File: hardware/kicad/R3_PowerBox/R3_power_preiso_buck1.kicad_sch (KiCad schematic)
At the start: 19 parts, among them U2 TPS54302DDCR

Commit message: Finalize R3 PowerBox pre-placement corrections
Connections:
- net N$13 renamed N$12

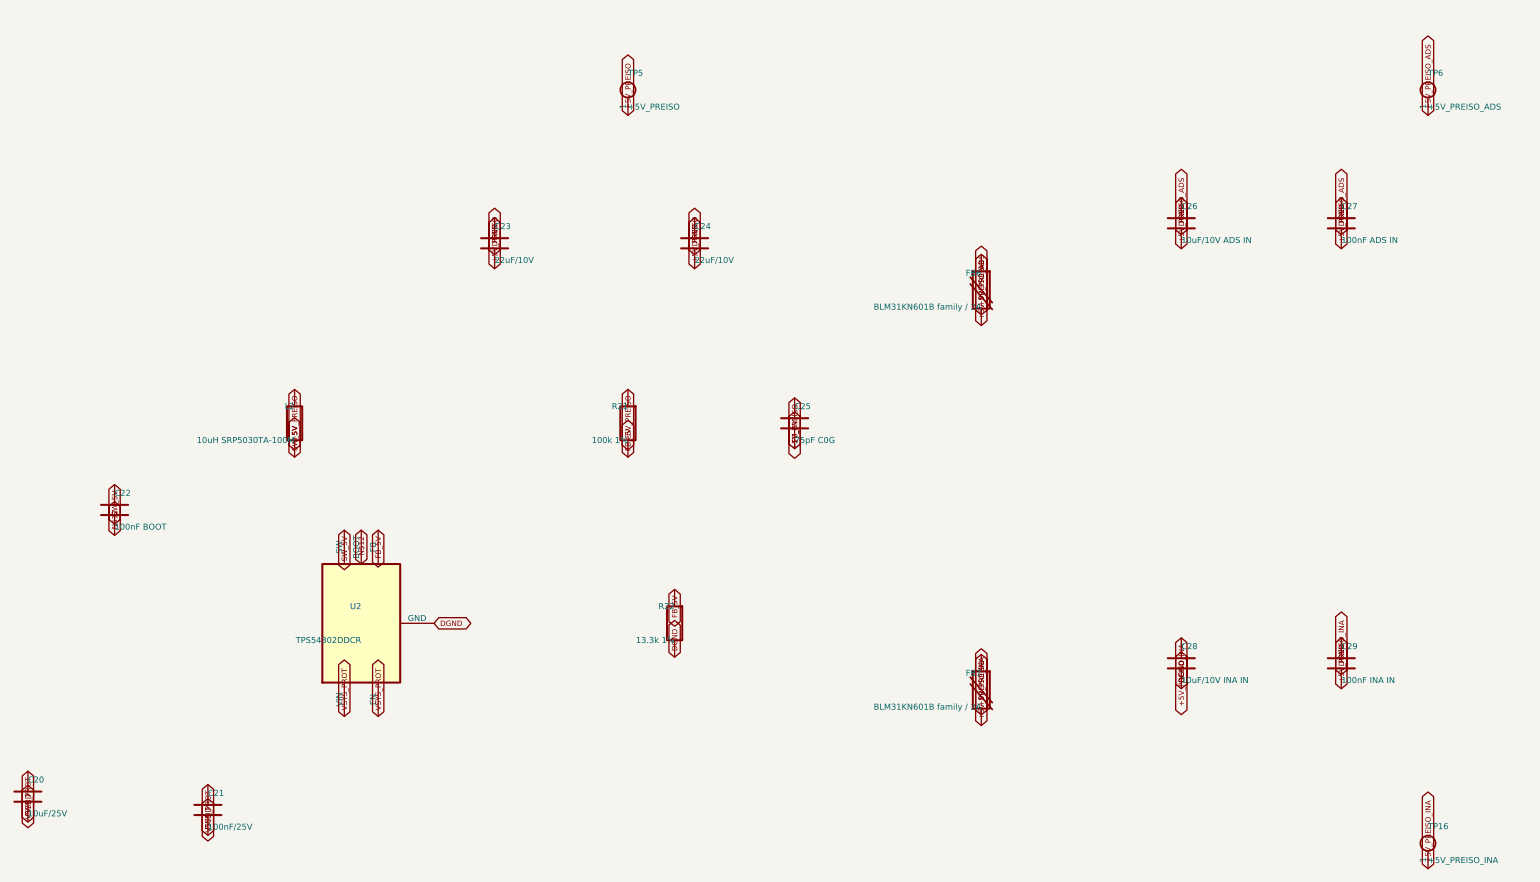
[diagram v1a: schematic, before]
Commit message: Finalize R3 PowerBox pre-routing placement
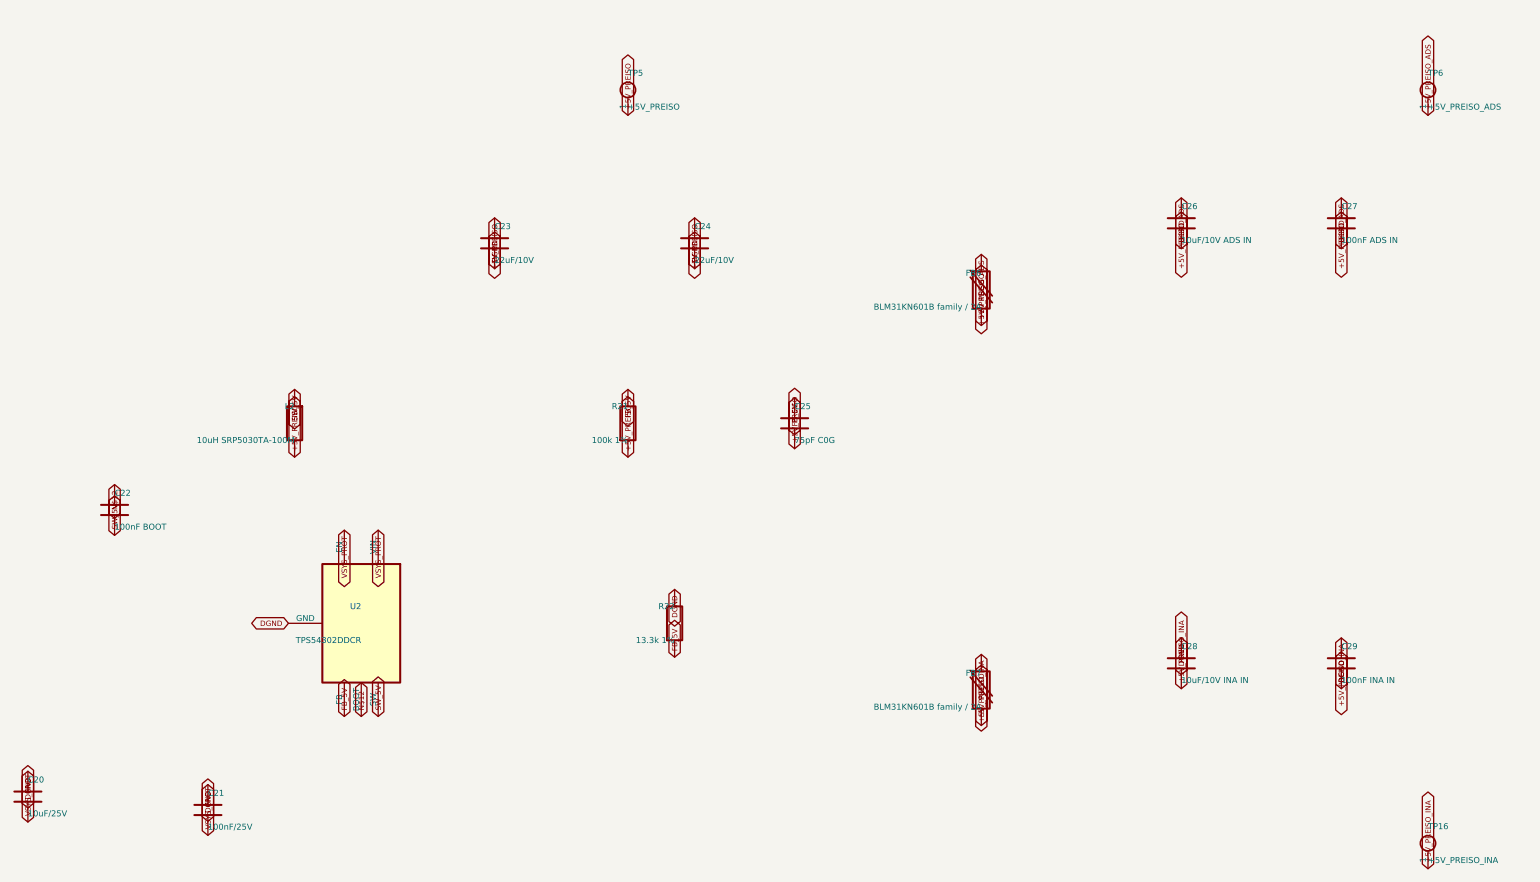
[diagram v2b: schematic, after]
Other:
- moved on the sheet: FB6, FB7, L2, R21, R22, U2

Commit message: Finalize R3 PowerBox user power controls
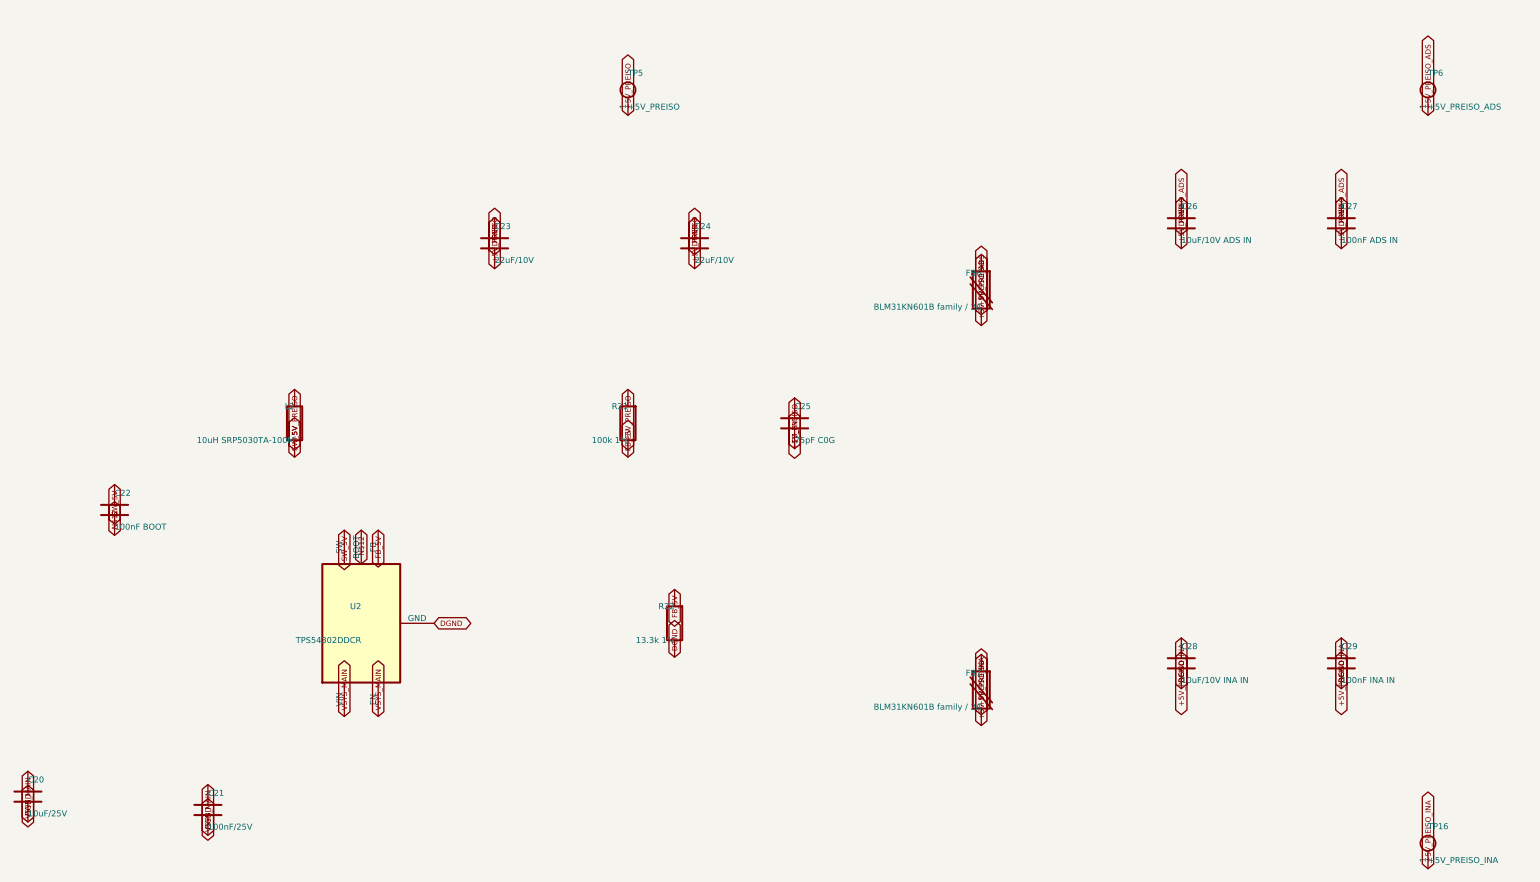
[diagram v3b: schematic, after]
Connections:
- net VSYS_PROT renamed VSYS_MAIN
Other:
- moved on the sheet: FB6, FB7, L2, R21, R22, U2

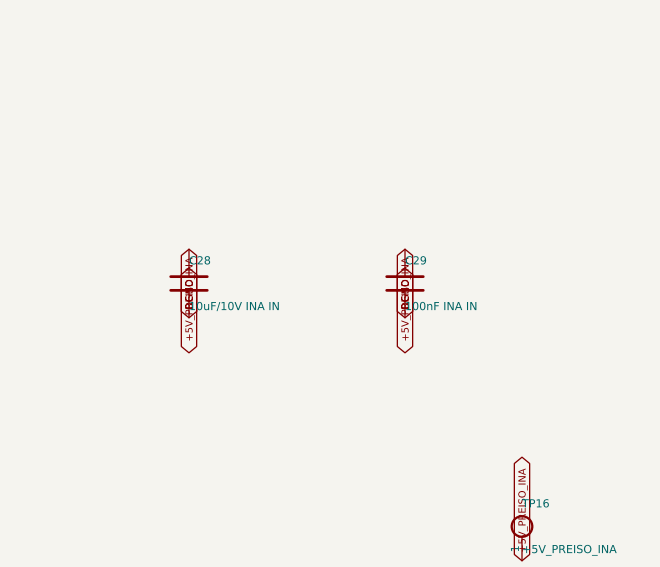
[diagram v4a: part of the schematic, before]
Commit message: Finish R3 PowerBox routing checkpoint F and verification
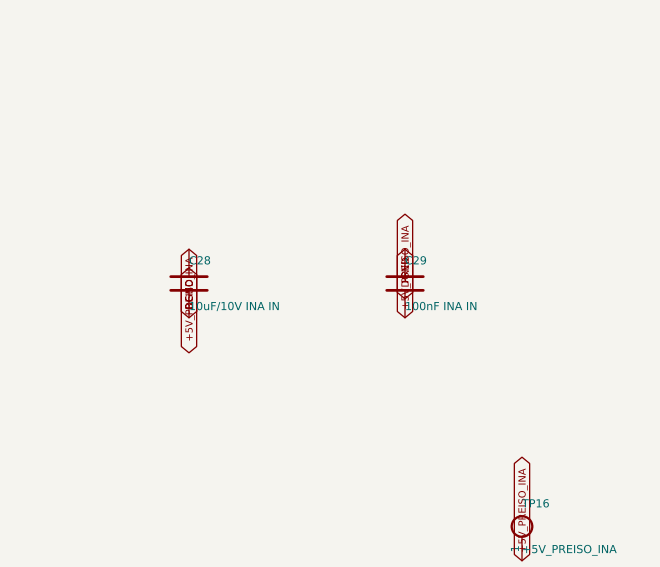
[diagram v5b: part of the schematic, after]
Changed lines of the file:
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@@
 	(global_label "+5V_PREISO_INA"
+		(shape bidirectional)
+		(at 252 131.81 90)
+		(effects
+			(font
+				(size 0.8 0.8)
+			)
+			(justify left)
+		)
+	)
+	(global_label "DGND"
 		(shape bidirectional)
 		(at 252 124.19 270)
@@
 			)
 			(justify right)
-		)
-	)
-	(global_label "DGND"
-		(shape bidirectional)
-		(at 252 131.81 90)
-		(effects
-			(font
-				(size 0.8 0.8)
-			)
-			(justify left)
 		)
 	)
@@
     (instances
       (project "SKiDL-Generated"
-        (path "/9be6bff1-dc85-4a48-94a9-d7223c5e518f/10a79bc1-5fff-5d5a-9873-ba1a5dc253c9"
+        (path "/c950aac3-a7f8-40a1-8854-63ca2e6194cc/10a79bc1-5fff-5d5a-9873-ba1a5dc253c9"
           (reference "U2")
           (unit 1)))))
@@
     (instances
       (project "SKiDL-Generated"
-        (path "/9be6bff1-dc85-4a48-94a9-d7223c5e518f/10a79bc1-5fff-5d5a-9873-ba1a5dc253c9"
+        (path "/c950aac3-a7f8-40a1-8854-63ca2e6194cc/10a79bc1-5fff-5d5a-9873-ba1a5dc253c9"
           (reference "L2")
           (unit 1)))))
@@
     (instances
       (project "SKiDL-Generated"
-        (path "/9be6bff1-dc85-4a48-94a9-d7223c5e518f/10a79bc1-5fff-5d5a-9873-ba1a5dc253c9"
+        (path "/c950aac3-a7f8-40a1-8854-63ca2e6194cc/10a79bc1-5fff-5d5a-9873-ba1a5dc253c9"
           (reference "C20")
           (unit 1)))))
@@
     (instances
       (project "SKiDL-Generated"
-        (path "/9be6bff1-dc85-4a48-94a9-d7223c5e518f/10a79bc1-5fff-5d5a-9873-ba1a5dc253c9"
+        (path "/c950aac3-a7f8-40a1-8854-63ca2e6194cc/10a79bc1-5fff-5d5a-9873-ba1a5dc253c9"
           (reference "C21")
           (unit 1)))))
@@
     (instances
       (project "SKiDL-Generated"
-        (path "/9be6bff1-dc85-4a48-94a9-d7223c5e518f/10a79bc1-5fff-5d5a-9873-ba1a5dc253c9"
+        (path "/c950aac3-a7f8-40a1-8854-63ca2e6194cc/10a79bc1-5fff-5d5a-9873-ba1a5dc253c9"
           (reference "C22")
           (unit 1)))))
@@
     (instances
       (project "SKiDL-Generated"
-        (path "/9be6bff1-dc85-4a48-94a9-d7223c5e518f/10a79bc1-5fff-5d5a-9873-ba1a5dc253c9"
+        (path "/c950aac3-a7f8-40a1-8854-63ca2e6194cc/10a79bc1-5fff-5d5a-9873-ba1a5dc253c9"
           (reference "C23")
           (unit 1)))))
@@
     (instances
       (project "SKiDL-Generated"
-        (path "/9be6bff1-dc85-4a48-94a9-d7223c5e518f/10a79bc1-5fff-5d5a-9873-ba1a5dc253c9"
+        (path "/c950aac3-a7f8-40a1-8854-63ca2e6194cc/10a79bc1-5fff-5d5a-9873-ba1a5dc253c9"
           (reference "C24")
           (unit 1)))))
@@
     (instances
       (project "SKiDL-Generated"
-        (path "/9be6bff1-dc85-4a48-94a9-d7223c5e518f/10a79bc1-5fff-5d5a-9873-ba1a5dc253c9"
+        (path "/c950aac3-a7f8-40a1-8854-63ca2e6194cc/10a79bc1-5fff-5d5a-9873-ba1a5dc253c9"
           (reference "R21")
           (unit 1)))))
@@
     (instances
       (project "SKiDL-Generated"
-        (path "/9be6bff1-dc85-4a48-94a9-d7223c5e518f/10a79bc1-5fff-5d5a-9873-ba1a5dc253c9"
+        (path "/c950aac3-a7f8-40a1-8854-63ca2e6194cc/10a79bc1-5fff-5d5a-9873-ba1a5dc253c9"
           (reference "R22")
           (unit 1)))))
@@
     (instances
       (project "SKiDL-Generated"
-        (path "/9be6bff1-dc85-4a48-94a9-d7223c5e518f/10a79bc1-5fff-5d5a-9873-ba1a5dc253c9"
+        (path "/c950aac3-a7f8-40a1-8854-63ca2e6194cc/10a79bc1-5fff-5d5a-9873-ba1a5dc253c9"
           (reference "C25")
           (unit 1)))))
@@
     (instances
       (project "SKiDL-Generated"
-        (path "/9be6bff1-dc85-4a48-94a9-d7223c5e518f/10a79bc1-5fff-5d5a-9873-ba1a5dc253c9"
+        (path "/c950aac3-a7f8-40a1-8854-63ca2e6194cc/10a79bc1-5fff-5d5a-9873-ba1a5dc253c9"
           (reference "FB6")
           (unit 1)))))
@@
     (instances
       (project "SKiDL-Generated"
-        (path "/9be6bff1-dc85-4a48-94a9-d7223c5e518f/10a79bc1-5fff-5d5a-9873-ba1a5dc253c9"
+        (path "/c950aac3-a7f8-40a1-8854-63ca2e6194cc/10a79bc1-5fff-5d5a-9873-ba1a5dc253c9"
           (reference "C26")
           (unit 1)))))
@@
     (instances
       (project "SKiDL-Generated"
-        (path "/9be6bff1-dc85-4a48-94a9-d7223c5e518f/10a79bc1-5fff-5d5a-9873-ba1a5dc253c9"
+        (path "/c950aac3-a7f8-40a1-8854-63ca2e6194cc/10a79bc1-5fff-5d5a-9873-ba1a5dc253c9"
           (reference "C27")
           (unit 1)))))
@@
     (instances
       (project "SKiDL-Generated"
-        (path "/9be6bff1-dc85-4a48-94a9-d7223c5e518f/10a79bc1-5fff-5d5a-9873-ba1a5dc253c9"
+        (path "/c950aac3-a7f8-40a1-8854-63ca2e6194cc/10a79bc1-5fff-5d5a-9873-ba1a5dc253c9"
           (reference "FB7")
           (unit 1)))))
@@
     (instances
       (project "SKiDL-Generated"
-        (path "/9be6bff1-dc85-4a48-94a9-d7223c5e518f/10a79bc1-5fff-5d5a-9873-ba1a5dc253c9"
+        (path "/c950aac3-a7f8-40a1-8854-63ca2e6194cc/10a79bc1-5fff-5d5a-9873-ba1a5dc253c9"
           (reference "C28")
           (unit 1)))))
@@
     (lib_id "R3_POWER_GEN:C")
     (at 252 128 0)
+    (mirror x)
     (unit 1)
     (exclude_from_sim no)
@@
     (instances
       (project "SKiDL-Generated"
-        (path "/9be6bff1-dc85-4a48-94a9-d7223c5e518f/10a79bc1-5fff-5d5a-9873-ba1a5dc253c9"
+        (path "/c950aac3-a7f8-40a1-8854-63ca2e6194cc/10a79bc1-5fff-5d5a-9873-ba1a5dc253c9"
           (reference "C29")
           (unit 1)))))
@@
     (instances
       (project "SKiDL-Generated"
-        (path "/9be6bff1-dc85-4a48-94a9-d7223c5e518f/10a79bc1-5fff-5d5a-9873-ba1a5dc253c9"
+        (path "/c950aac3-a7f8-40a1-8854-63ca2e6194cc/10a79bc1-5fff-5d5a-9873-ba1a5dc253c9"
           (reference "TP5")
           (unit 1)))))
@@
     (instances
       (project "SKiDL-Generated"
-        (path "/9be6bff1-dc85-4a48-94a9-d7223c5e518f/10a79bc1-5fff-5d5a-9873-ba1a5dc253c9"
+        (path "/c950aac3-a7f8-40a1-8854-63ca2e6194cc/10a79bc1-5fff-5d5a-9873-ba1a5dc253c9"
           (reference "TP6")
           (unit 1)))))
@@
     (instances
       (project "SKiDL-Generated"
-        (path "/9be6bff1-dc85-4a48-94a9-d7223c5e518f/10a79bc1-5fff-5d5a-9873-ba1a5dc253c9"
+        (path "/c950aac3-a7f8-40a1-8854-63ca2e6194cc/10a79bc1-5fff-5d5a-9873-ba1a5dc253c9"
           (reference "TP16")
           (unit 1)))))

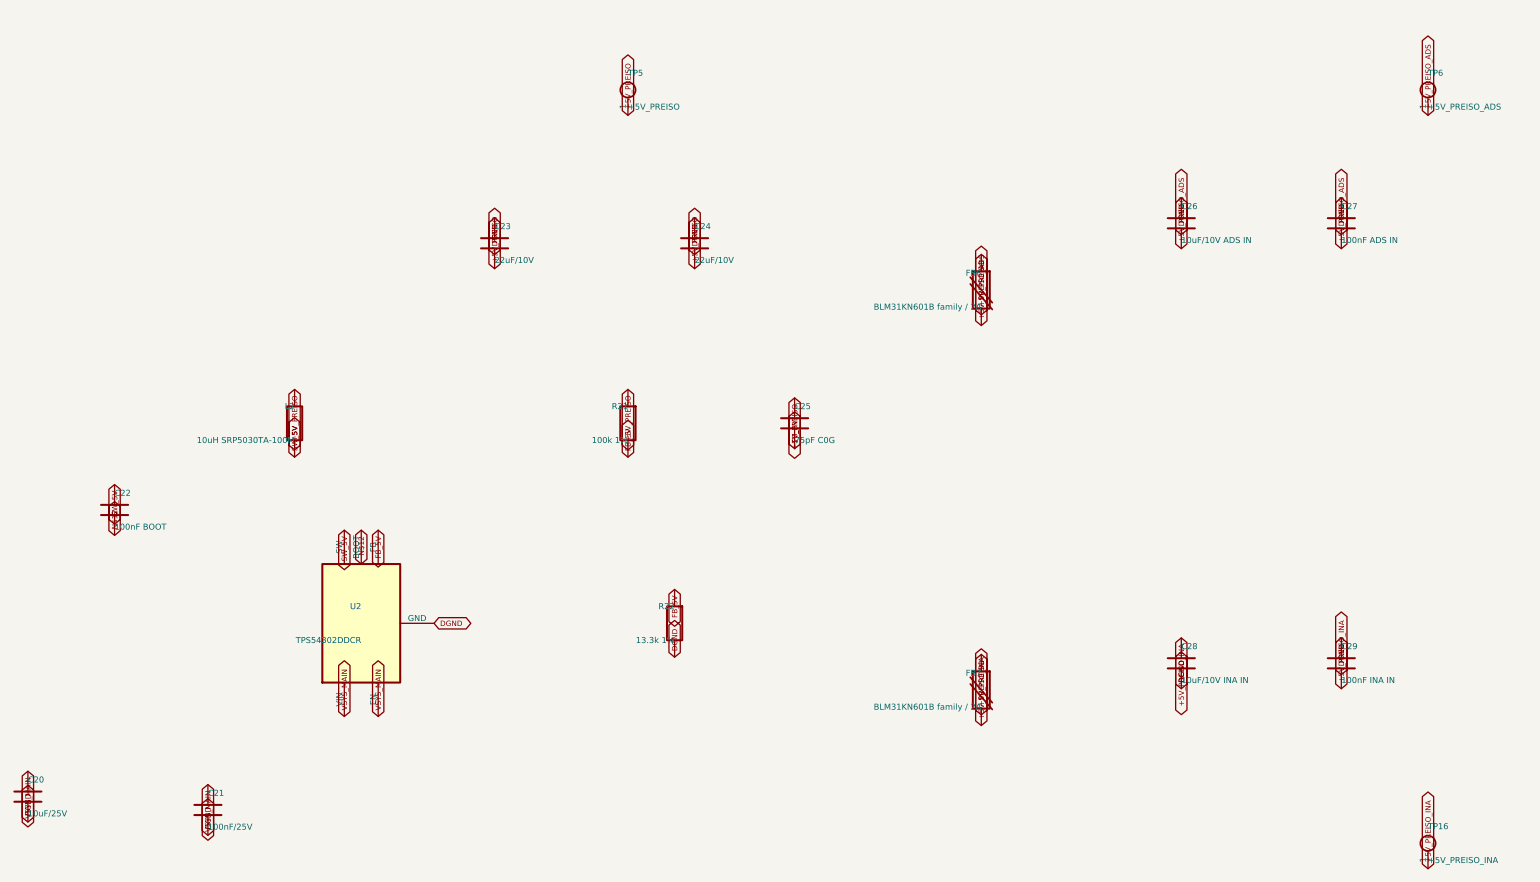
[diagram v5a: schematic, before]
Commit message: Rev.A review fixes: initial schematic and component corrections
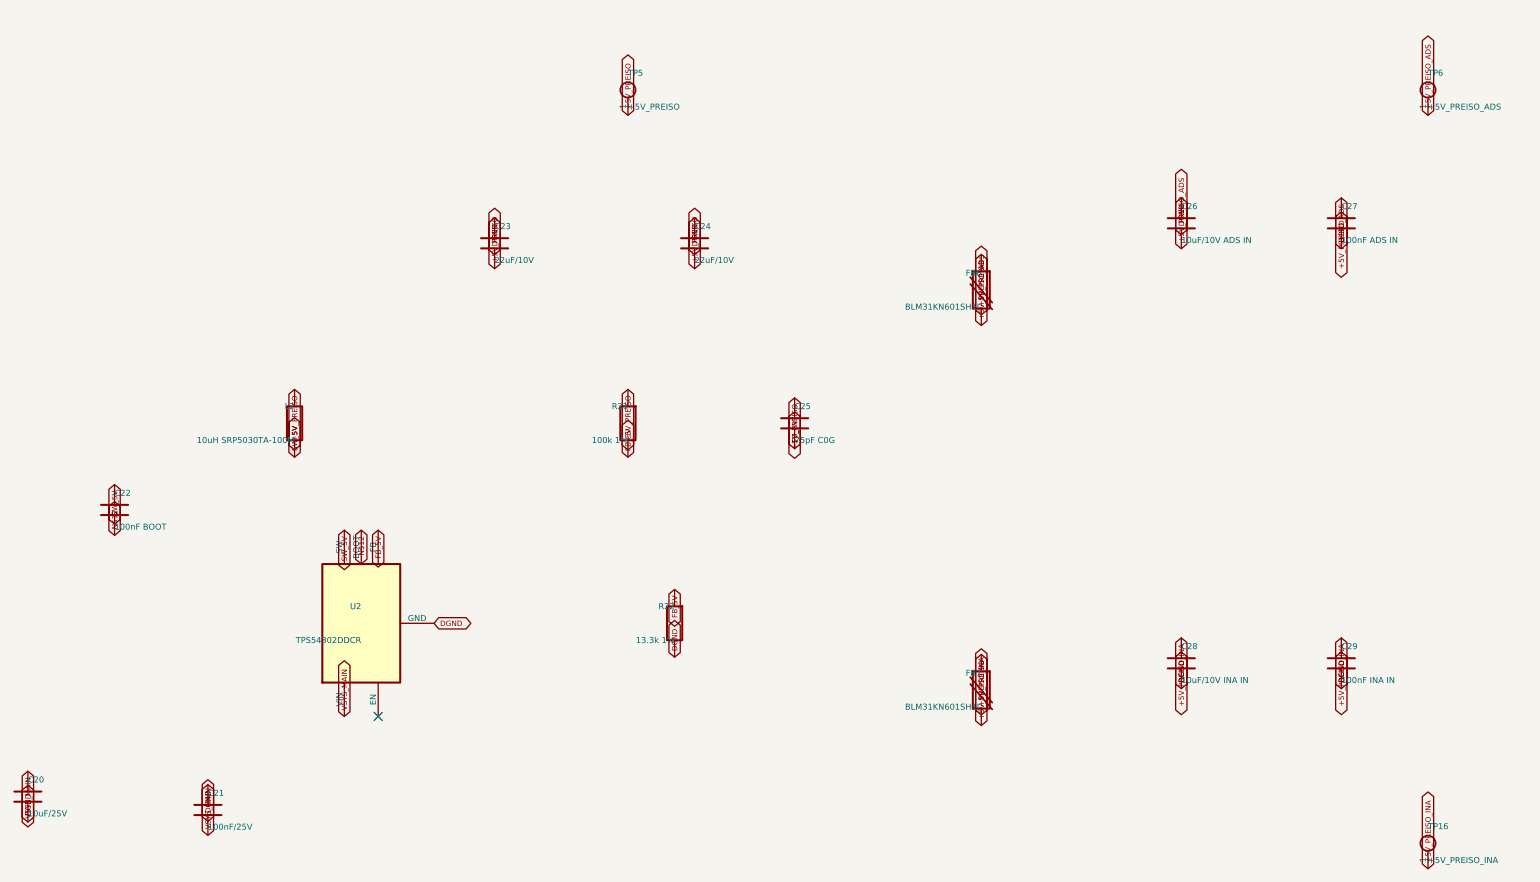
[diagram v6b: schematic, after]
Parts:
- FB6, FB7: value BLM31KN601B family / 2A -> BLM31KN601SH1L
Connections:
- net VSYS_MAIN: no longer U2.5 (EN)
- no-connect marks 0 -> 1
